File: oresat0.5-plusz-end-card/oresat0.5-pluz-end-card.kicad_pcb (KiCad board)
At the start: 4 copper layers, 99.8 x 94.6 mm, 35 parts, among them J1 J-SAMTEC-TFM-120-01-L-D-RA, J2 Harwin M55-7101242R, J3 Harwin M55-7101242R, J4 Harwin M55-7101242R, J5 Harwin M55-7101242R, J6 Conn_Coaxial

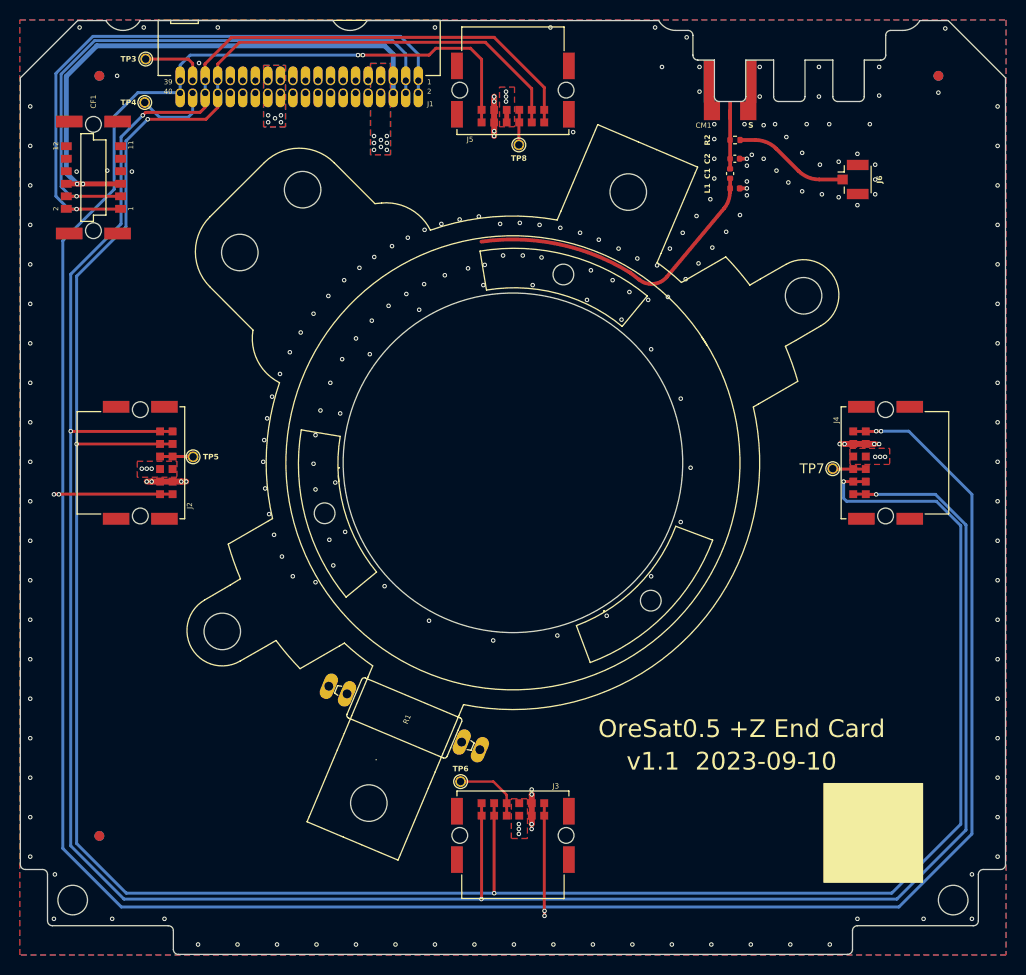
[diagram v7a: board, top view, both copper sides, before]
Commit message: Oresat0.5 +Z end card: v1.1. Updated to latest KiCAD.
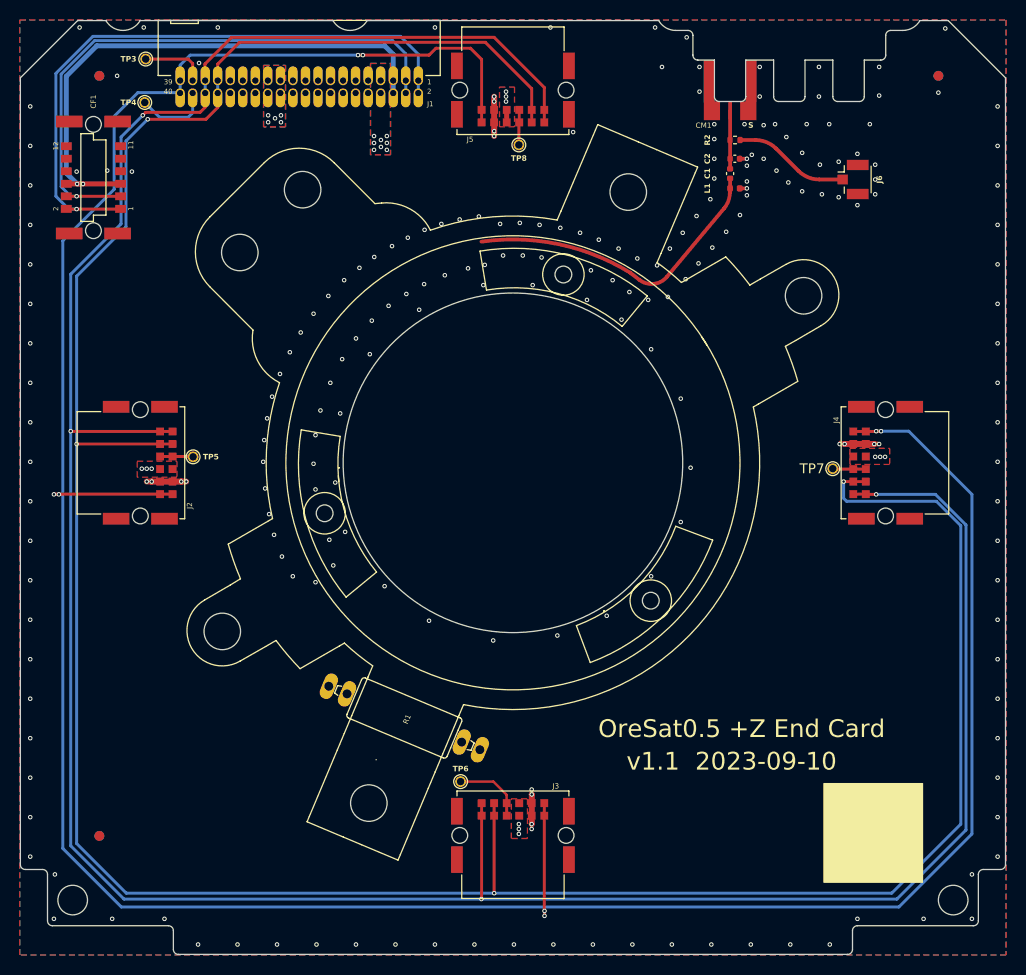
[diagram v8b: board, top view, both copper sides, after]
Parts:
- HW5, HW6, HW7: footprint oresat-misc:Hole-2.1mm-NPTH -> oresat-misc:M1.6 Mounting Hole
